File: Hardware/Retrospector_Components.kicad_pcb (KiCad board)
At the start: 4 copper layers, 60 x 110 mm, 122 parts, among them J1 SWD_Header, J2 Eurorack_10_pin_power, J3 Conn_01x08_Male, J4 Conn_01x08_Male, J5 Conn_01x08_Male, J6 Conn_01x08_Male, J7 USB_B_Micro, U1 STM32H743ZITx, U2 IS42S16400J-xC, U3 PCM5100APW, U4 SSI2164, U5 MCP6004, U6 MCP6004, U7 TL074, U8 LM1117-3.3, Y1 8MHz 20pF

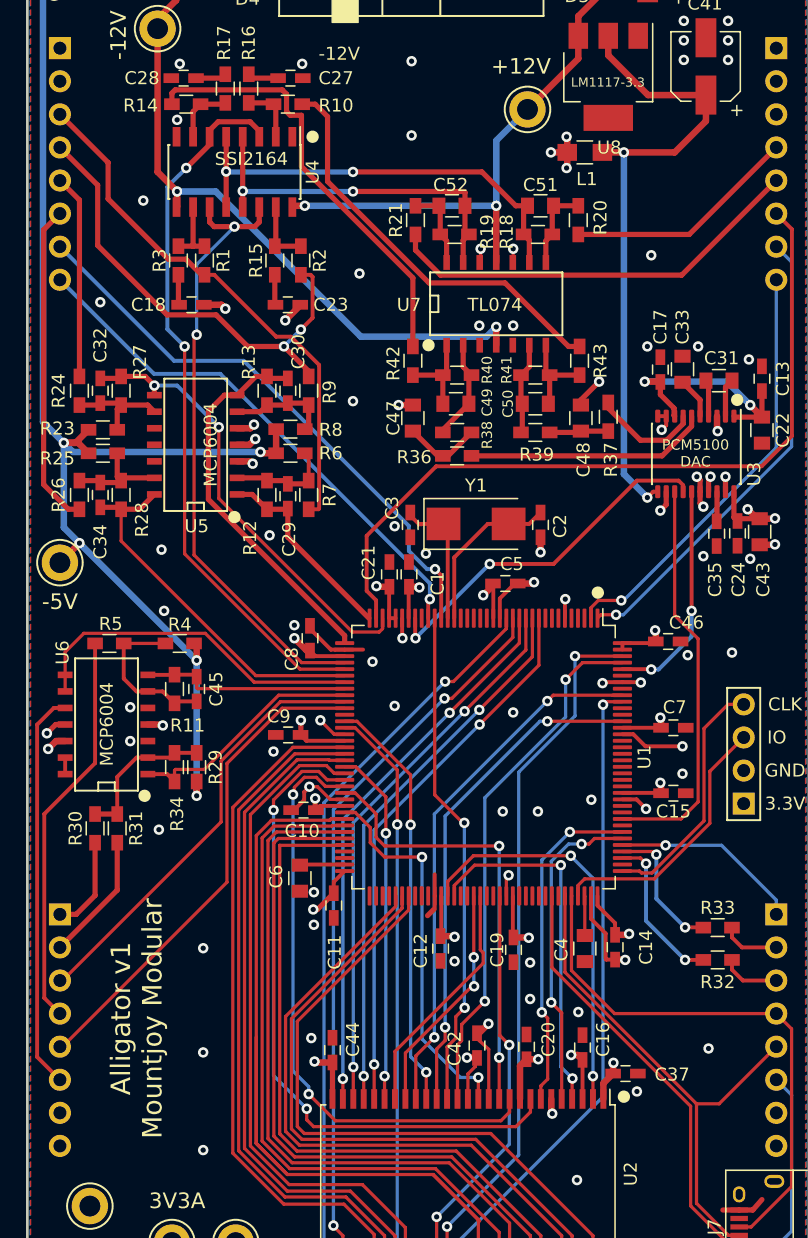
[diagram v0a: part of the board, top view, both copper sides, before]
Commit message: Renamed project files; work on panel PCB and 3d Models
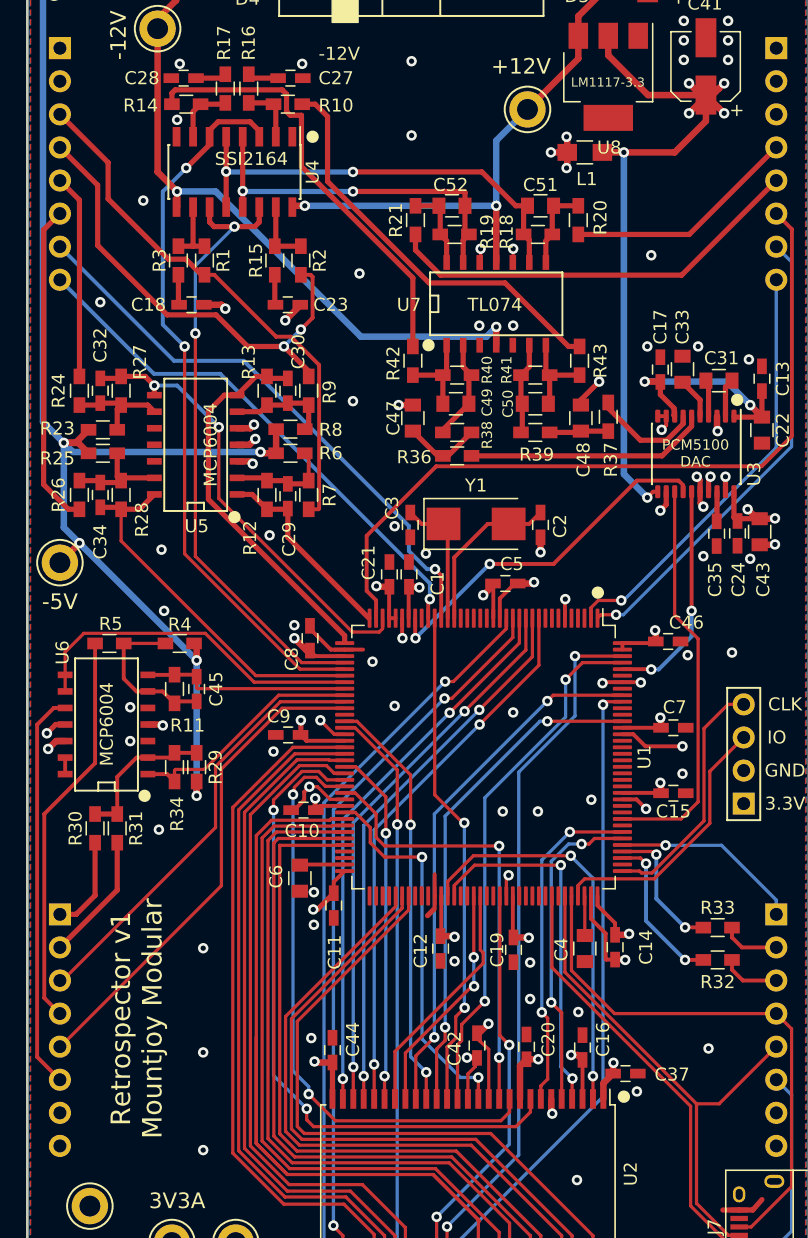
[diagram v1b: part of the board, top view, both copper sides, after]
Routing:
- net +3V3: track 134.5 -> 141.8 mm, vias 25 -> 29
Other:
- board text added: "Retrospector v1 Mountjoy Modular"
- board text removed: "Alligator v1 Mountjoy Modular"

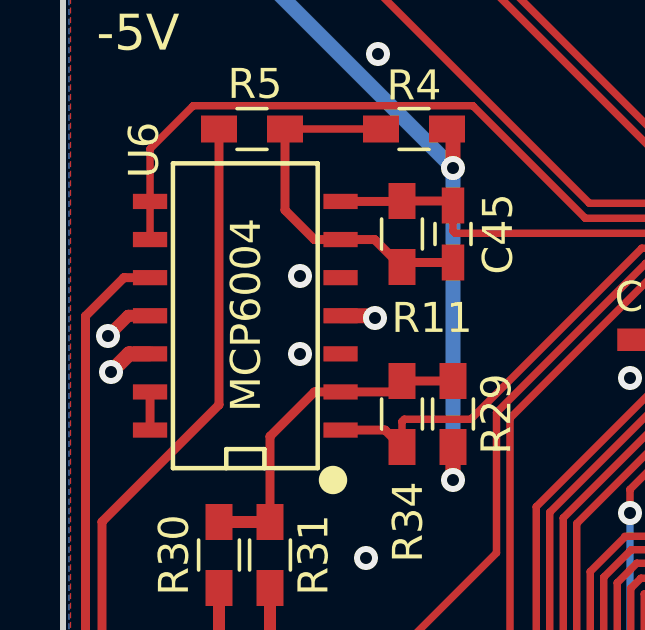
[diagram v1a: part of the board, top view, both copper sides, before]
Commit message: Panel and Control PCB Updates
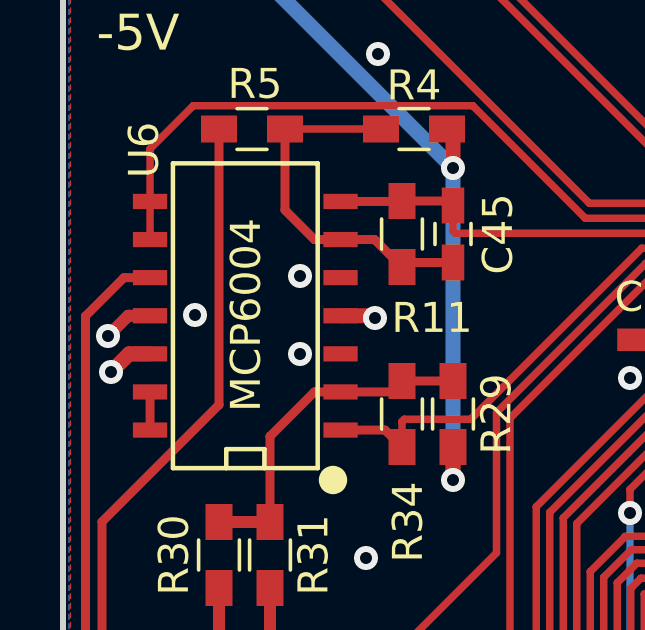
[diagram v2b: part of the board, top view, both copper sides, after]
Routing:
- net GND: vias 101 -> 102
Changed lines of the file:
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@@
     (thickness 1.6)
     (drawings 21)
-    (tracks 1248)
+    (tracks 1249)
     (zones 0)
     (modules 122)
@@
   (via (at 154.8 53.7) (size 0.8) (drill 0.4) (layers F.Cu B.Cu) (net 1))
   (via (at 152.3 140.3) (size 0.8) (drill 0.4) (layers F.Cu B.Cu) (net 1))
+  (via (at 104.4 115.4) (size 0.8) (drill 0.4) (layers F.Cu B.Cu) (net 1))
   (segment (start 132.775 102.6) (end 135.35 100.025) (width 0.3) (layer F.Cu) (net 2))
   (segment (start 135.35 100.025) (end 136.95 100.025) (width 0.3) (layer F.Cu) (net 2) (status 20))

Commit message: Final changes to PCBs for manufacture
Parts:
- added C53: 10uF, Capacitors_SMD:C_0805, F.Cu at (125.2, 93.8)
- C31, C33, C4, C6: footprint Capacitors_SMD:C_0805 -> Capacitors_SMD:C_0603_HandSoldering
- C39, C40: footprint Capacitors_SMD:CP_Elec_5x5.3 -> Capacitors_SMD:CP_Elec_6.3x5.3
- C41: footprint Capacitors_SMD:CP_Elec_5x5.3 -> Capacitors_SMD:CP_Elec_6.3x7.7
- Y1: footprint Crystals:Crystal_SMD_0603-2pin_6.0x3.5mm_HandSoldering -> Crystals:Crystal_SMD_5032-2pin_5.0x3.2mm_HandSoldering
- moved TP6 1.89 mm to (108.4, 63.0)
- moved TP1 1.77 mm to (106.1, 153.6)
- moved C2 1.00 mm to (140.4, 100.0)
- moved C39 0.79 mm to (147.8, 55.5)
- moved Y1 0.45 mm to (134.9, 100.0)
- moved D4 0.30 mm to (117.1, 56.0)
- moved C40 0.23 mm to (111.2, 55.6)
- moved C36 0.20 mm to (153.3, 56.2)
- moved C33 0.11 mm to (150.4, 88.2)
- moved C41 0.10 mm to (152.1, 65.0)
- moved D3 0.10 mm to (142.1, 56.2)
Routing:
- net VEE: track 64.9 -> 68.5 mm
- net GND: track 82.2 -> 84.1 mm, vias 102 -> 104
- net VCC: track 57.0 -> 55.3 mm
- net Net-(C2-Pad1): track 12.7 -> 14.4 mm
- net +3V3: track 141.8 -> 143.3 mm
- net +3.3VA: track 30.3 -> 31.4 mm, vias 9 -> 10

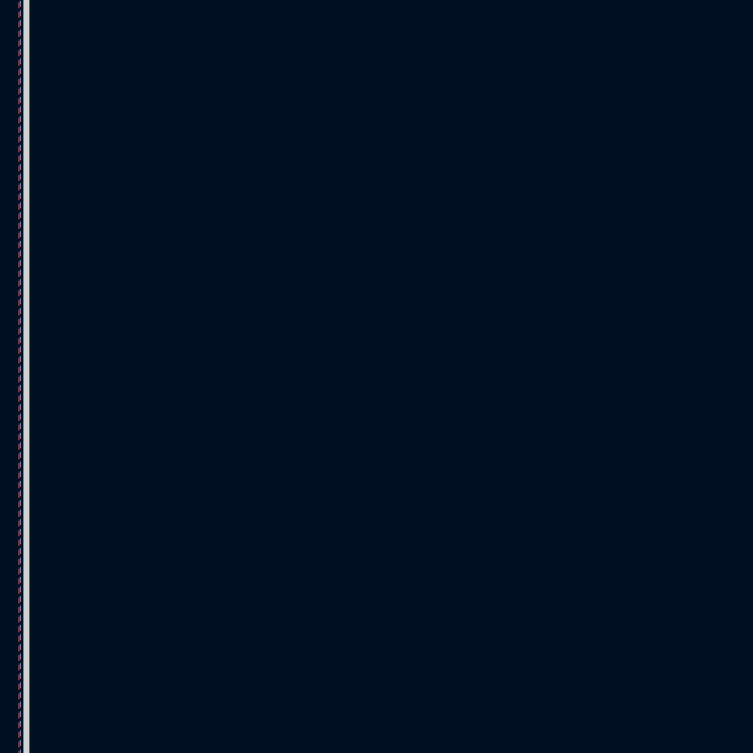
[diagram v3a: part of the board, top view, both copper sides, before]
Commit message: Reduced clock speed; started implementing SDRAM code; ADC updates
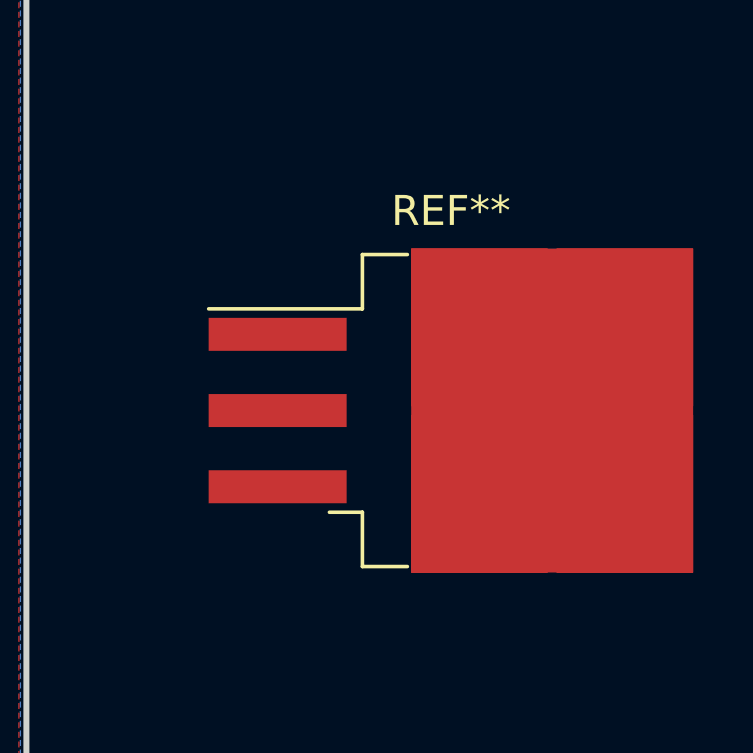
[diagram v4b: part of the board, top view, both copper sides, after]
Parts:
- added REF**: TO-263-3_TabPin2, TO_SOT_Packages_SMD:TO-263-3_TabPin2, F.Cu at (174.2, 65.8)
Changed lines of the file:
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@@
     (tracks 1261)
     (zones 0)
-    (modules 123)
+    (modules 124)
     (nets 176)
   )
@@
     (0 F.Cu signal)
     (1 Ground.Fill power hide)
-    (2 Power.Rails power hide)
+    (2 Power.Rails power)
     (31 B.Cu signal)
     (32 B.Adhes user)
@@
     (uvia_drill 0.1)
   )
+  (module TO_SOT_Packages_SMD:TO-263-3_TabPin2 (layer F.Cu)
+    (at 174.15 65.78)
+    (descr "TO-263 / D2PAK / DDPAK SMD package, http://www.infineon.com/cms/en/product/packages/PG-TO263/PG-TO263-3-1/")
+    (tags "D2PAK DDPAK TO-263 D2PAK-3 TO-263-3 SOT-404")
+    (attr smd)
+    (fp_text reference REF** (at 0 -6.65) (layer F.SilkS)
+      (effects (font (size 1 1) (thickness 0.15)))
+    )
+    (fp_text value TO-263-3_TabPin2 (at 0 6.65) (layer F.Fab)
+      (effects (font (size 1 1) (thickness 0.15)))
+    )
+    (fp_line (start 6.5 -5) (end 7.5 -5) (layer F.Fab) (width 0.1))
+    (fp_line (start 7.5 -5) (end 7.5 5) (layer F.Fab) (width 0.1))
+    (fp_line (start 7.5 5) (end 6.5 5) (layer F.Fab) (width 0.1))
+    (fp_line (start 6.5 -5) (end 6.5 5) (layer F.Fab) (width 0.1))
+    (fp_line (start 6.5 5) (end -2.75 5) (layer F.Fab) (width 0.1))
+    (fp_line (start -2.75 5) (end -2.75 -4) (layer F.Fab) (width 0.1))
+    (fp_line (start -2.75 -4) (end -1.75 -5) (layer F.Fab) (width 0.1))
+    (fp_line (start -1.75 -5) (end 6.5 -5) (layer F.Fab) (width 0.1))
+    (fp_line (start -2.75 -3.04) (end -7.45 -3.04) (layer F.Fab) (width 0.1))
+    (fp_line (start -7.45 -3.04) (end -7.45 -2.04) (layer F.Fab) (width 0.1))
+    (fp_line (start -7.45 -2.04) (end -2.75 -2.04) (layer F.Fab) (width 0.1))
+    (fp_line (start -2.75 -0.5) (end -7.45 -0.5) (layer F.Fab) (width 0.1))
+    (fp_line (start -7.45 -0.5) (end -7.45 0.5) (layer F.Fab) (width 0.1))
+    (fp_line (start -7.45 0.5) (end -2.75 0.5) (layer F.Fab) (width 0.1))
+    (fp_line (start -2.75 2.04) (end -7.45 2.04) (layer F.Fab) (width 0.1))
+    (fp_line (start -7.45 2.04) (end -7.45 3.04) (layer F.Fab) (width 0.1))
+    (fp_line (start -7.45 3.04) (end -2.75 3.04) (layer F.Fab) (width 0.1))
+    (fp_line (start -1.45 -5.2) (end -2.95 -5.2) (layer F.SilkS) (width 0.12))
+    (fp_line (start -2.95 -5.2) (end -2.95 -3.39) (layer F.SilkS) (width 0.12))
+    (fp_line (start -2.95 -3.39) (end -8.075 -3.39) (layer F.SilkS) (width 0.12))
+    (fp_line (start -1.45 5.2) (end -2.95 5.2) (layer F.SilkS) (width 0.12))
+    (fp_line (start -2.95 5.2) (end -2.95 3.39) (layer F.SilkS) (width 0.12))
+    (fp_line (start -2.95 3.39) (end -4.05 3.39) (layer F.SilkS) (width 0.12))
+    (fp_line (start -8.32 -5.65) (end -8.32 5.65) (layer F.CrtYd) (width 0.05))
+    (fp_line (start -8.32 5.65) (end 8.32 5.65) (layer F.CrtYd) (width 0.05))
+    (fp_line (start 8.32 5.65) (end 8.32 -5.65) (layer F.CrtYd) (width 0.05))
+    (fp_line (start 8.32 -5.65) (end -8.32 -5.65) (layer F.CrtYd) (width 0.05))
+    (fp_text user %R (at 0 0) (layer F.Fab)
+      (effects (font (size 1 1) (thickness 0.15)))
+    )
+    (pad 1 smd rect (at -5.775 -2.54) (size 4.6 1.1) (layers F.Cu F.Paste F.Mask))
+    (pad 2 smd rect (at -5.775 0) (size 4.6 1.1) (layers F.Cu F.Paste F.Mask))
+    (pad 3 smd rect (at -5.775 2.54) (size 4.6 1.1) (layers F.Cu F.Paste F.Mask))
+    (pad 2 smd rect (at 3.375 0) (size 9.4 10.8) (layers F.Cu F.Mask))
+    (pad 2 smd rect (at 5.8 2.775) (size 4.55 5.25) (layers F.Cu F.Paste))
+    (pad 2 smd rect (at 0.95 -2.775) (size 4.55 5.25) (layers F.Cu F.Paste))
+    (pad 2 smd rect (at 5.8 -2.775) (size 4.55 5.25) (layers F.Cu F.Paste))
+    (pad 2 smd rect (at 0.95 2.775) (size 4.55 5.25) (layers F.Cu F.Paste))
+    (model ${KISYS3DMOD}/TO_SOT_Packages_SMD.3dshapes/TO-263-3_TabPin2.wrl
+      (at (xyz 0 0 0))
+      (scale (xyz 1 1 1))
+      (rotate (xyz 0 0 0))
+    )
+  )
   (module Custom_Footprints:JLC_SMT_Tooling_Hole (layer F.Cu)

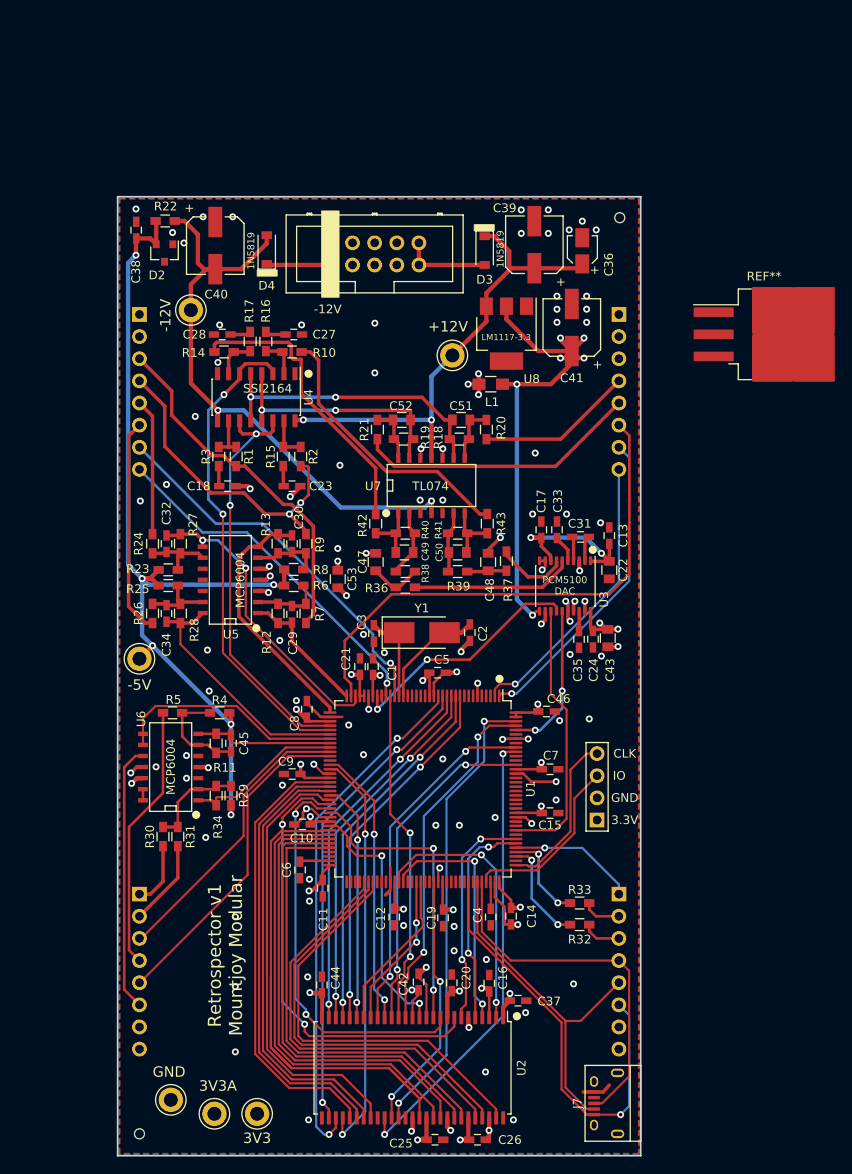
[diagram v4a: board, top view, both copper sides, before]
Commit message: Started updating schematics and pcb layout for rev 2 changes; updated and tested clock pin to use production assignment
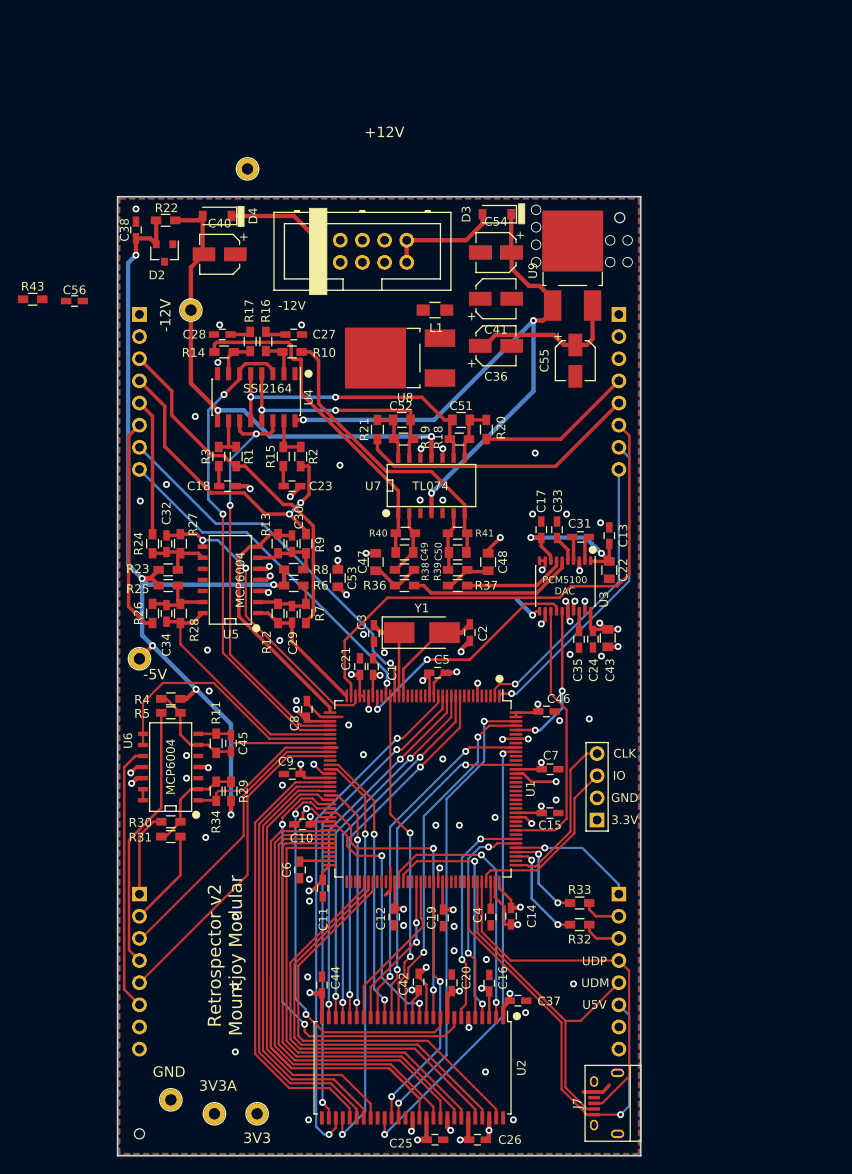
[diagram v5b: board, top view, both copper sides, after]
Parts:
- removed R42: 1k, Resistors_SMD:R_0603_HandSoldering
- removed REF**: TO-263-3_TabPin2, TO_SOT_Packages_SMD:TO-263-3_TabPin2
- added C54: 22uF, Capacitors_SMD:CP_Elec_4x5.8, F.Cu at (143.4, 56.4)
- added C55: 22uF, Capacitors_SMD:CP_Elec_4x5.8, F.Cu at (152.5, 68.8)
- added C56: 5nF, Capacitors_SMD:C_0603_HandSoldering, F.Cu at (95.0, 62.0)
- added U9: BA7807FP-E2, TO_SOT_Packages_SMD:TO-252-2_Rectifier, F.Cu at (152.2, 57.9)
- C36: value 10uF -> 22uF; footprint Capacitors_SMD:CP_Elec_3x5.3 -> Capacitors_SMD:CP_Elec_4x5.8
- C39: footprint Capacitors_SMD:CP_Elec_6.3x5.3 -> Capacitors_SMD:CP_Elec_4x5.8; moved to B.Cu
- C40: footprint Capacitors_SMD:CP_Elec_6.3x5.3 -> Capacitors_SMD:CP_Elec_4x5.8
- C41: value 47uF -> 22uF; footprint Capacitors_SMD:CP_Elec_6.3x7.7 -> Capacitors_SMD:CP_Elec_4x5.8
- R43: value 1k -> 100R
- TP1, TP2, TP3, TP4, TP5, TP6: footprint Measurement_Points:Test_Point_Keystone_5005-5009_Compact -> Custom_Footprints:1.3mm_Test_Point
- U2: value IS42S16400J-xC -> IS42S16800F-7TLI
- U8: value LM1117-3.3 -> NCV1117DT33T5G; footprint TO_SOT_Packages_SMD:SOT-223 -> TO_SOT_Packages_SMD:TO-252-2_Rectifier
- moved R43 58.2 mm to (90.2, 61.8), turned to 0 degrees
- moved TP5 31.8 mm to (114.9, 46.8)
- moved C36 14.7 mm to (143.4, 67.1), turned to 0 degrees
- moved U8 12.5 mm to (132.4, 68.5), turned to 180 degrees
- moved L1 10.6 mm to (136.4, 63.0)
- moved C41 9.30 mm to (143.4, 61.7), turned to 0 degrees
- moved D4 6.88 mm to (111.4, 52.2), turned to 180 degrees
- moved R37 6.26 mm to (139.0, 94.6), turned to 0 degrees
- moved R4 5.82 mm to (106.1, 107.6)
- moved C39 4.49 mm to (143.4, 56.4), turned to 180 degrees
- moved D3 4.40 mm to (143.5, 52.0), turned to 180 degrees
- moved R30 1.92 mm to (106.1, 121.7), turned to 180 degrees
- moved J2 1.43 mm to (123.0, 57.5)
- moved C40 1.12 mm to (111.7, 56.6), turned to 180 degrees
- moved R31 0.80 mm to (106.1, 123.4), turned to 0 degrees
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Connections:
- C36 pad 1: VCC -> /+7V
- C38 pad 1: AREF_-5 -> GND
- C38 pad 2: GND -> AREF_-5
- C49 pad 1: Net-(C49-Pad1) -> /DAC_OUT_AMP_L
- C50 pad 1: Net-(C50-Pad1) -> /DAC_OUT_AMP_R
- R40 pad 1: Net-(C49-Pad1) -> /DAC_OUT_AMP_L
- R41 pad 1: Net-(C50-Pad1) -> /DAC_OUT_AMP_R
- R43 pad 1: /DAC_OUT_AMP_R -> Net-(C56-Pad1)
- R43 pad 2: Net-(C50-Pad1) -> Net-(R43-Pad2)
- U4 pad 1: Net-(U4-Pad1) -> Net-(R43-Pad2)
- U7 pad 1: Net-(C49-Pad1) -> /DAC_OUT_AMP_L
- U7 pad 11: VCC -> VEE
- U7 pad 4: VEE -> VCC
- U7 pad 7: Net-(C50-Pad1) -> /DAC_OUT_AMP_R
- U8 pad 1: GND -> /+7V
- U8 pad 2: +3V3 -> GND
- U8 pad 3: VCC -> +3V3
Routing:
- net +3V3: track 143.3 -> 88.6 mm, vias 29 -> 24
- net VCC: track 55.3 -> 75.5 mm, vias 2 -> 3
- net /+7V: track 0.00 -> 18.0 mm
- net VEE: track 68.5 -> 57.0 mm
- net Net-(C50-Pad1): track 6.96 -> 0.00 mm
- net Net-(C49-Pad1): track 6.92 -> 0.00 mm
- net /DAC_OUT_AMP_L: track 33.8 -> 39.4 mm
- net +3.3VA: track 31.4 -> 27.7 mm, vias 10 -> 7
- net /DAC_OUT_R: track 8.31 -> 11.8 mm
- net -12V: track 10.2 -> 13.6 mm
- net +12V: track 10.2 -> 13.1 mm
- net /DAC_OUT_AMP_R: track 31.9 -> 34.5 mm
- net /CLOCK_SCALED: track 26.6 -> 29.1 mm
- net /MIX_CV: track 7.35 -> 9.86 mm
- net AREF_-5: track 104.3 -> 105.7 mm
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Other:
- board text added: "Retrospector v2 Mountjoy Modular"
- board text added: "U5V"
- board text added: "UDM"
- board text added: "UDP"
- board text removed: "Retrospector v1 Mountjoy Modular"
